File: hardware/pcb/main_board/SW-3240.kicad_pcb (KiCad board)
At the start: 2 copper layers, 177.8 x 119.4 mm, 106 parts, among them J1 AUX_MIC_IN, J10 PWR, J11 BAT, J12 Channel 1, J13 Channel 2, J14 Channel 3, J15 Channel 4, J16 CH_1, J17 CH_2, J18 CH_3, J19 CH_4, J2 AUX_LINE_IN, J3 MIC, J4 LINE IN, J5 ICSP, J6 FP_IO, J7 MIC_IN_R, J8 FTDI, J9 SW-32MA, Q1 BSS138, Q2 BSS138, SW1 PWR_SW, U1 MCP4728, U2 ATmega328PB-AU, U3 TPS5430DDA, U4 TPS5430DDA, U5 LM2941, U6 NCP1117-3.3, Y1 16MHz

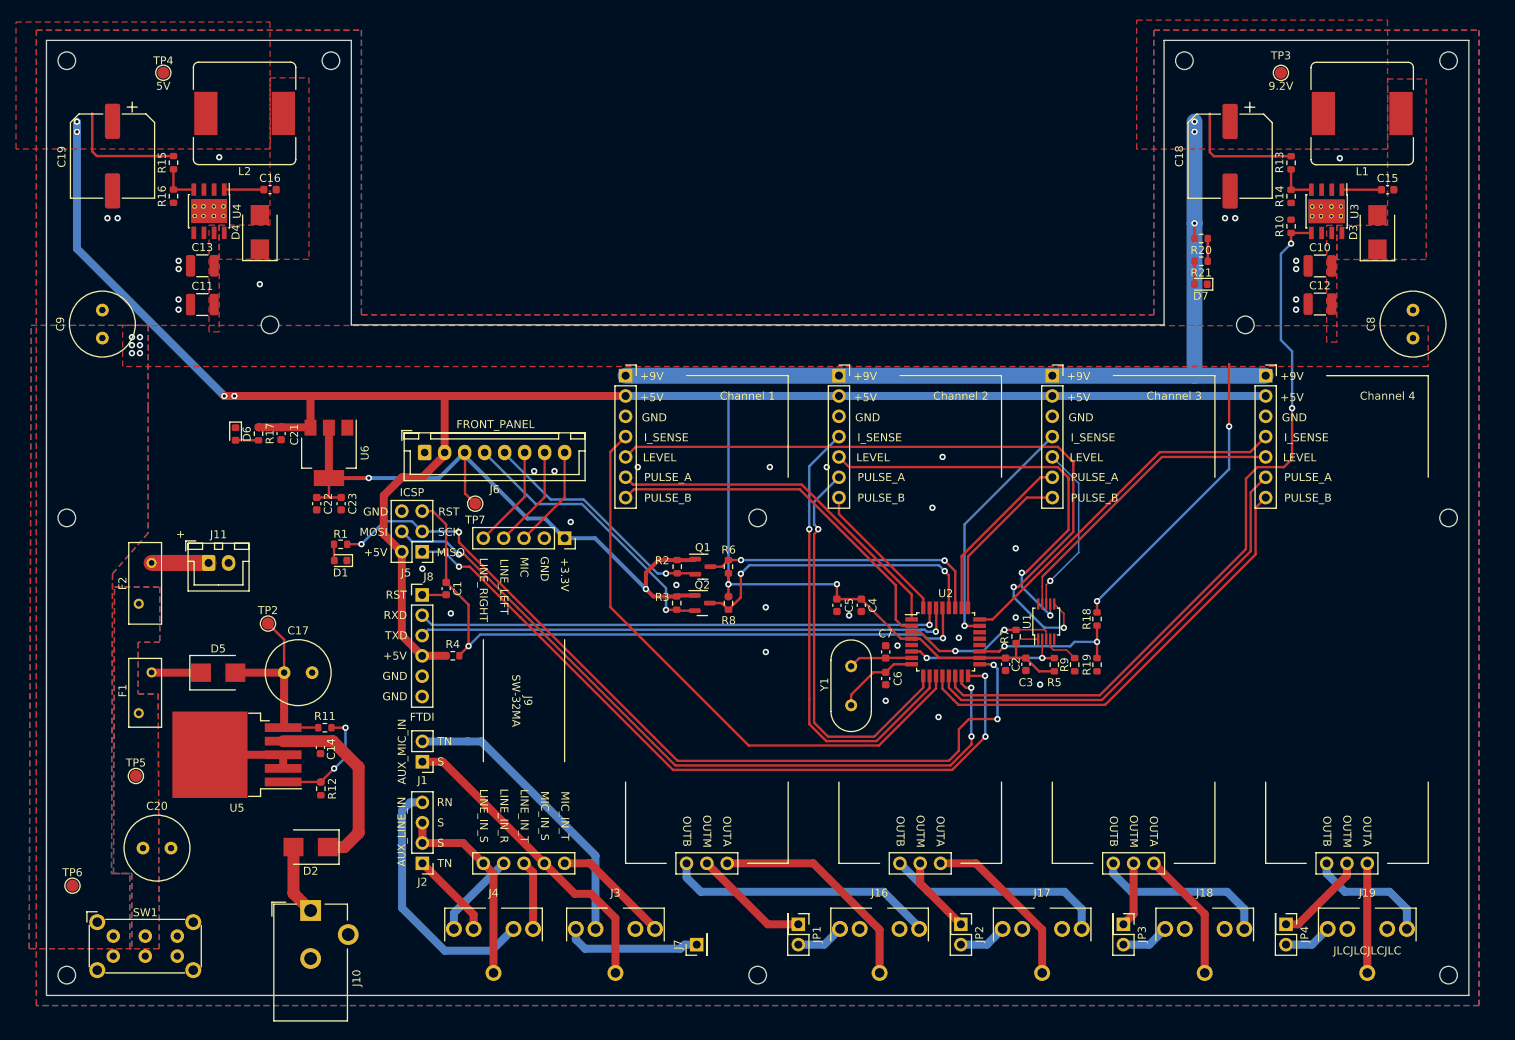
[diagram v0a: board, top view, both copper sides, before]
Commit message: update part numbers
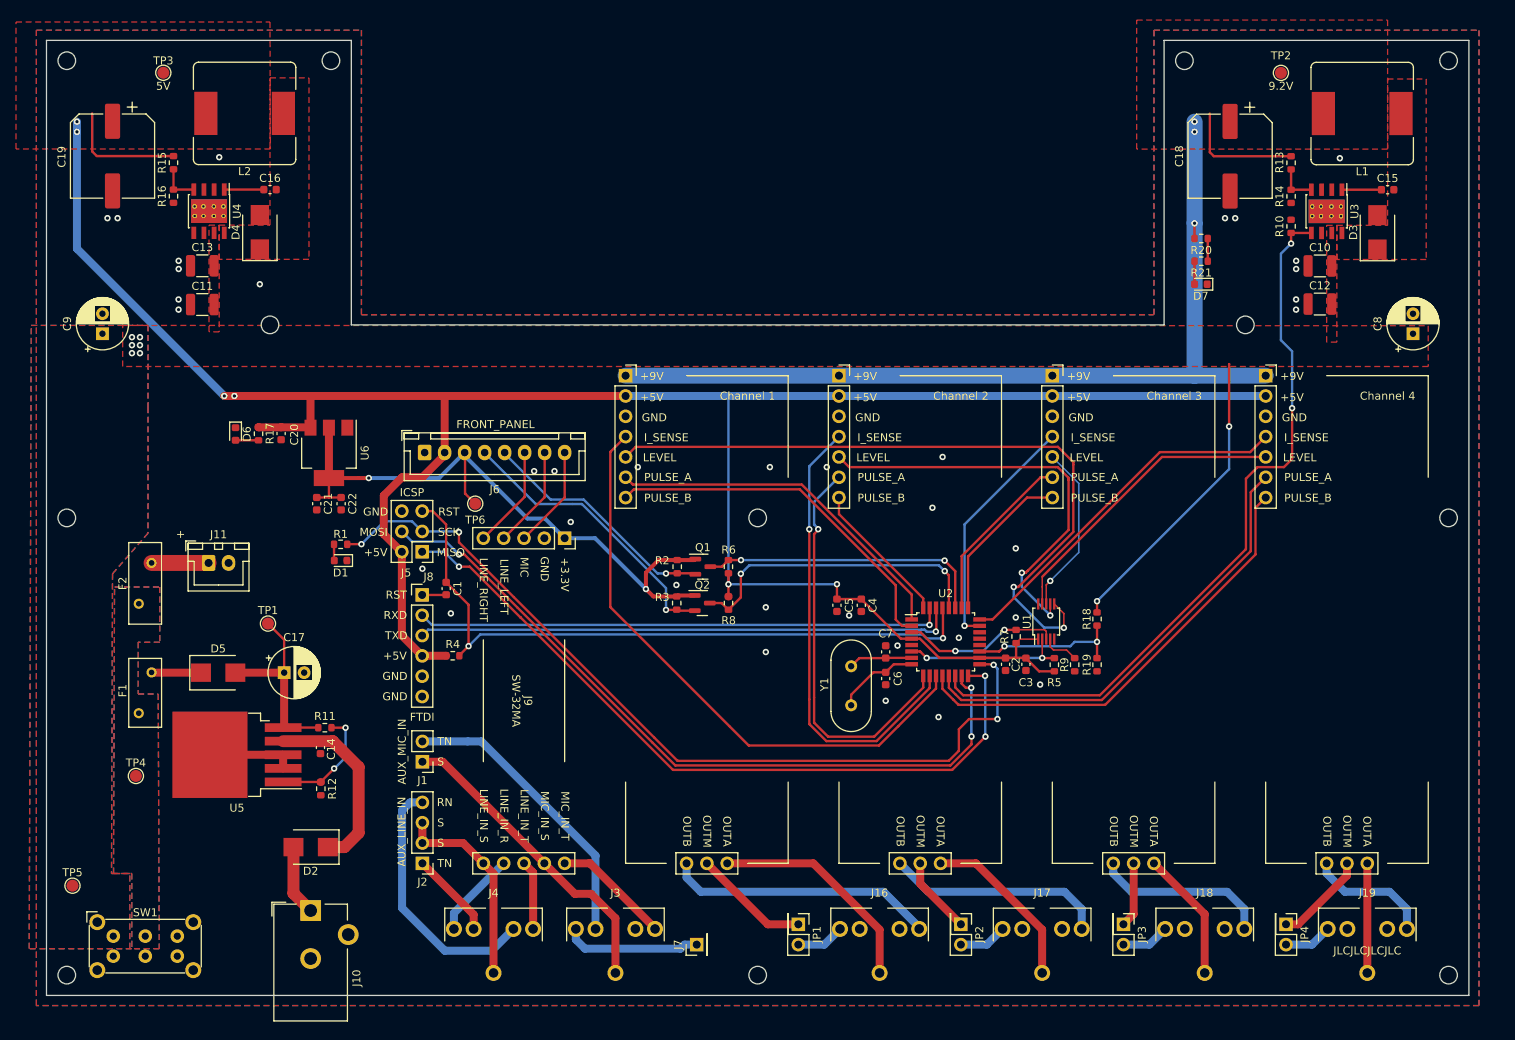
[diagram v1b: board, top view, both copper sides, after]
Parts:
- removed the C20 at (78.1, 131.4)
- C17, C8, C9: footprint Capacitor_THT:C_Radial_D8.0mm_H11.5mm_P3.50mm -> Capacitor_THT:CP_Radial_D6.3mm_P2.50mm
- moved C9 0.54 mm to (73.0, 67.1)
- moved C8 0.54 mm to (236.9, 67.1)
- renumbered C21 to C20, C22 to C21, C23 to C22, TP2 to TP1, TP3 to TP2, TP4 to TP3, TP5 to TP4, TP6 to TP5, TP7 to TP6

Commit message: redesign
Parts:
- removed C22, C5: 100nF, Capacitor_SMD:C_0603_1608Metric
- removed the C3 at (188.5, 108.5)
- removed the C4 at (167.9, 101.1)
- removed the C6 at (170.9, 110.2)
- removed C7: 22pF, Capacitor_SMD:C_0603_1608Metric
- removed the D1 at (102.8, 95.5)
- removed the J1 at (113.0, 120.7)
- removed the J2 at (113.0, 133.3)
- removed the J7 at (147.3, 143.5)
- removed Q2: BSS138, Package_TO_SOT_SMD:SOT-23
- removed R18: 10K, Resistor_SMD:R_0603_1608Metric
- removed R19: 4.7K, Resistor_SMD:R_0603_1608Metric
- removed the R2 at (144.9, 96.3)
- removed R20: 1K, Resistor_SMD:R_0603_1608Metric
- removed the R3 at (144.8, 100.8)
- removed the R4 at (116.8, 107.4)
- removed the R5 at (192.0, 108.5)
- removed the R6 at (151.3, 96.3)
- removed the R7 at (187.2, 105.0)
- removed the R8 at (151.3, 100.8)
- removed the R9 at (194.6, 108.5)
- removed the U2 at (178.4, 105.7)
- removed Y1: 16MHz, Crystal:Crystal_HC49-4H_Vertical
- added C17: 10uF, Capacitor_SMD:C_0603_1608Metric, F.Cu at (175.8, 101.6)
- added C18: 100nF, Capacitor_SMD:C_0603_1608Metric, F.Cu at (172.7, 101.6)
- added C19: 100nF, Capacitor_SMD:C_0603_1608Metric, F.Cu at (158.6, 98.1)
- added J3: AUX_ALT, Connector_PinHeader_2.54mm:PinHeader_2x04_P2.54mm_Vertical, F.Cu at (122.2, 139.0)
- added J4: ESPFlash, Connector_IDC:IDC-Header_2x03_P2.54mm_Vertical, F.Cu at (94.0, 104.1)
- added J9: BAT, Connector_JST:JST_XH_B2B-XH-A_1x02_P2.50mm_Vertical, F.Cu at (81.3, 80.1)
- added R10: 10K, Resistor_SMD:R_0603_1608Metric, F.Cu at (230.4, 87.9)
- added R11: 10K, Resistor_SMD:R_0603_1608Metric, F.Cu at (230.4, 92.2)
- added R12: 4.7K, Resistor_SMD:R_0603_1608Metric, F.Cu at (227.3, 92.2)
- added R14: 4.7K, Resistor_SMD:R_0603_1608Metric, F.Cu at (179.1, 107.5)
- added R15: 4.7K, Resistor_SMD:R_0603_1608Metric, F.Cu at (181.9, 107.5)
- added R16: 10K, Resistor_SMD:R_0603_1608Metric, F.Cu at (184.9, 107.5)
- added R17: 10K, Resistor_SMD:R_0603_1608Metric, F.Cu at (161.4, 98.1)
- added U6: Pico, SaawLib:RPi_Pico_SMD, F.Cu at (217.2, 106.7)
- added U7: MCP4728, Package_SO:MSOP-10_3x3mm_P0.5mm, F.Cu at (180.3, 101.6)
- added U8: ADS1015, Package_SO:TSSOP-10_3x3mm_P0.5mm, F.Cu at (165.1, 101.6)
- C1: value 100nF -> 10uF
- C2: value 10uF -> 100nF
- D4: renamed from D5; value SSB44-E3 -> locked
- D6: renamed from D7; value BLUE -> locked
- J1: renamed from J3; value MIC -> AUX1
- J10: value PWR -> SERIAL; footprint SaawLib:BarrelJack_CUI_PJ-102AH_Horizontal -> Connector_PinHeader_2.54mm:PinHeader_1x06_P2.54mm_Vertical
- J11: value BAT -> DEBUG; footprint Connector_JST:JST_XH_B2B-XH-A_1x02_P2.50mm_Vertical -> Connector_PinHeader_2.54mm:PinHeader_1x03_P2.54mm_Vertical
- J2: renamed from J4; value LINE IN -> AUX2
- J5: value ICSP -> FRONT_PANEL; footprint Connector_PinHeader_2.54mm:PinHeader_2x03_P2.54mm_Vertical -> Connector_PinHeader_2.54mm:PinHeader_2x08_P2.54mm_Vertical
- J6: value FP_IO -> DISPLAY; footprint Connector_JST:JST_XH_B8B-XH-A_1x08_P2.50mm_Vertical -> Connector_PinHeader_2.54mm:PinHeader_1x10_P2.54mm_Vertical
- J7: renamed from J9; value SW-32MA -> locked
- J8: value FTDI -> PWR; footprint Connector_PinHeader_2.54mm:PinHeader_1x06_P2.54mm_Vertical -> SaawLib:BarrelJack_CUI_PJ-102AH_Horizontal
- JP1, JP2, JP3, JP4: footprint Connector_PinHeader_2.54mm:PinHeader_2x01_P2.54mm_Vertical -> Connector_PinHeader_2.54mm:PinHeader_1x02_P2.54mm_Vertical
- Q1: value BSS138 -> DMG2301L-7
- R1: value 1K -> 10K
- R13: renamed from R21; value 1K -> 1.5K
- TP3: value 5V -> locked
- U1: value MCP4728 -> ESP32-WROOM-32D; footprint Package_SO:MSOP-10_3x3mm_P0.5mm -> RF_Module:ESP32-WROOM-32
- moved Q1 95.0 mm to (239.7, 121.4), turned to -90 degrees
- moved C2 87.5 mm to (100.6, 89.2), turned to 90 degrees
- moved U1 76.3 mm to (114.9, 96.7), turned to 0 degrees
- moved J10 66.3 mm to (133.3, 82.5)
- moved J11 47.4 mm to (133.3, 101.6)
- moved J8 42.1 mm to (99.1, 139.5)
- moved R2 41.3 mm to (234.5, 93.0), turned to 0 degrees
- moved J2 33.0 mm to (154.9, 146.1)
- moved J6 32.5 mm to (103.5, 113.0), turned to 90 degrees
- moved TP6 30.2 mm to (89.7, 84.3)
- moved J5 25.5 mm to (94.0, 77.5), turned to 0 degrees
- moved C12 25.3 mm to (85.3, 132.6), turned to -90 degrees
- moved R1 23.4 mm to (119.8, 109.5)
- moved R4 21.4 mm to (79.3, 128.3), turned to 0 degrees
- moved U5 21.0 mm to (82.5, 91.4), turned to 90 degrees
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- renumbered C15 to C10, C16 to C11, C17 to C12, C18 to C13, C19 to C14, C20 to C15, C21 to C16, C8 to C3, C9 to C4, C11 to C6, C13 to C8, C14 to C9, D2 to D1, D3 to D2, D4 to D3, D6 to D5, H12 to H1, H3 to H10, H2 to H11, H1 to H12, H10 to H2, H8 to H3, H6 to H4, H11 to H5, H9 to H6, H5 to H8, H4 to H9, R10 to R2, R11 to R3, R12 to R4, R13 to R5, R14 to R6, R15 to R7, R16 to R8, R17 to R9, U3 to U2, U4 to U3, U5 to U4, U6 to U5, C10 to locked, C12 to locked
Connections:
- net /CH_PSU_EN renamed /REG_EN
- net Net-(J1-Pad1) renamed /AUX1S
- net Net-(J2-Pad2) renamed /AUX2S
- C1 pad 1: /RESET -> +3V3
- C1 pad 2: Net-(C1-Pad2) -> GND
- C2 pad 1: +5V -> +3V3
- D1 pad 2: /PSU/VIN -> Net-(D1-Pad2)
- F2 pad 2: /PSU/VBAT -> Net-(F2-Pad2)
- J1 pad R: Net-(J3-PadR) -> Net-(J1-PadR)
- J1 pad RN: unconnected-(J3-PadRN) -> /AUX1RN
- J1 pad T: Net-(J3-PadT) -> Net-(J1-PadT)
- J1 pad TN: Net-(J1-Pad2) -> /AUX1TN
- J10 pad 1: /PSU/VIN -> GND
- J10 pad 2: GND -> unconnected-(J10-Pad2)
- J10 pad 3: (no net) -> unconnected-(J10-Pad3)
- J11 pad 1: /PSU/VBAT -> /Output/SWCLK
- J12 pad 2: +5V -> +3V3
- J12 pad 4: /CHA_I_SENSE -> /Output/CH1_SENSE
- J12 pad 5: /CHA_LEVEL -> /Output/CH1_LVL
- J12 pad 6: /CHA_PULSE_A -> /Output/CH1_PA
- J12 pad 7: /CHA_PULSE_B -> /Output/CH1_PB
- J13 pad 2: +5V -> +3V3
- J13 pad 4: /CHB_I_SENSE -> /Output/CH2_SENSE
- J13 pad 5: /CHB_LEVEL -> /Output/CH2_LVL
- J13 pad 6: /CHB_PULSE_A -> /Output/CH2_PA
- J13 pad 7: /CHB_PULSE_B -> /Output/CH2_PB
- J14 pad 2: +5V -> +3V3
- J14 pad 4: /CHC_I_SENSE -> /Output/CH3_SENSE
- J14 pad 5: /CHC_LEVEL -> /Output/CH3_LVL
- J14 pad 6: /CHC_PULSE_A -> /Output/CH3_PA
- J14 pad 7: /CHC_PULSE_B -> /Output/CH3_PB
- J15 pad 2: +5V -> +3V3
- J15 pad 4: /CHD_I_SENSE -> /Output/CH4_SENSE
- J15 pad 5: /CHD_LEVEL -> /Output/CH4_LVL
- J15 pad 6: /CHD_PULSE_A -> /Output/CH4_PA
- J15 pad 7: /CHD_PULSE_B -> /Output/CH4_PB
- J2 pad R: Net-(J4-PadR) -> Net-(J2-PadR)
- J2 pad RN: Net-(J2-Pad4) -> /AUX2RN
- J2 pad T: Net-(J4-PadT) -> Net-(J2-PadT)
- J2 pad TN: Net-(J2-Pad1) -> /AUX2TN
- J5 pad 1: /MISO -> GND
- J5 pad 2: +5V -> /LVL_1
- J5 pad 3: /SCK -> +3V3
- J5 pad 4: /MOSI -> /LVL_2
- J5 pad 5: /RESET -> +5V
- J5 pad 6: GND -> /LVL_3
- J6 pad 2: +5V -> +3V3
- J6 pad 3: +3V3 -> /LCD_RST
- J6 pad 4: /SCL_3V3 -> /LCD_DC
- J6 pad 5: /SDA_3V3 -> /CARD_CS
- J6 pad 6: /LINE_RIGHT -> /LCD_CS
- J6 pad 7: /LINE_LEFT -> /MOSI
- J6 pad 8: /MIC -> /SCK
- J7 pad 1: +3V3 -> GND
- J7 pad 2: GND -> +3V3
- J7 pad 3: /MIC -> /AUX1T
- J7 pad 4: /LINE_LEFT -> /AUX1R
- J7 pad 5: /LINE_RIGHT -> /AUX2T
- J7 pad 6: Net-(J3-PadT) -> /AUX2R
- J7 pad 8: Net-(J4-PadT) -> Net-(J1-PadR)
- J7 pad 9: Net-(J4-PadR) -> Net-(J1-PadT)
- J8 pad 1: Net-(C1-Pad2) -> Net-(D1-Pad2)
- J8 pad 2: /RXD -> GND
- J8 pad 3: /TXD -> unconnected-(J8-Pad3)
- Q1 pad 1: +3V3 -> Net-(Q1-Pad1)
- Q1 pad 2: /SDA_3V3 -> Net-(Q1-Pad2)
- Q1 pad 3: /SDA -> +3V3
- R1 pad 1: /SCK -> /IO2
- R1 pad 2: Net-(D1-Pad2) -> GND
- R13 pad 2: Net-(R20-Pad1) -> +9V
- U1 pad 1: +5V -> GND
- U1 pad 10: GND -> /AUX2T
- U1 pad 2: /DAC_SCL -> +3V3
- U1 pad 3: /DAC_SDA -> /EN
- U1 pad 4: Net-(R9-Pad2) -> /LVL_1
- U1 pad 5: unconnected-(U1-Pad5) -> /LVL_2
- U1 pad 6: /CHA_LEVEL -> /LVL_3
- U1 pad 7: /CHB_LEVEL -> /LVL_4
- U1 pad 8: /CHC_LEVEL -> /AUX1T
- U1 pad 9: /CHD_LEVEL -> /AUX1R
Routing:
- net +3V3: track 82.4 -> 399.8 mm, vias 2 -> 3
- net +5V: track 318.7 -> 89.3 mm, vias 6 -> 3
- net /CIO3: track 0.00 -> 164.9 mm, vias 0 -> 3
- net /CIO2: track 0.00 -> 159.4 mm, vias 0 -> 3
- net /CIO1: track 0.00 -> 152.8 mm, vias 0 -> 1
- net /Output/TXD: track 0.00 -> 117.5 mm
- net /Output/RXD: track 0.00 -> 115.5 mm
- net /CS: track 0.00 -> 105.9 mm, vias 0 -> 2
- net /CHA_LEVEL: track 88.9 -> 0.00 mm, vias 2 -> 0
- net /RESET: track 85.6 -> 0.00 mm, vias 2 -> 0
- net /CHA_I_SENSE: track 74.5 -> 0.00 mm
- net /Output/CH1_PA: track 0.00 -> 70.6 mm
- net /Output/CH1_PB: track 0.00 -> 67.9 mm
- net /Output/CH4_SENSE: track 0.00 -> 67.6 mm, vias 0 -> 1
- net /Output/SWCLK: track 0.00 -> 64.8 mm
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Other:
- board text added: "SW-3240 Main Board Rev 1"
